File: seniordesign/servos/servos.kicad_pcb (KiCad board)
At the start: 2 copper layers, 77.5 x 38.1 mm, 24 parts, among them CON1 USB-MICRO-B, P1 SERVO_PWMS, U1 FT234XD, U2 MSP430G2153, U3 ADP151AUJZ-3.3-R7, U4 SN74LV1T04, U5 SN74LV1T04, U6 SN74LV1T04, U7 SN74LV1T04

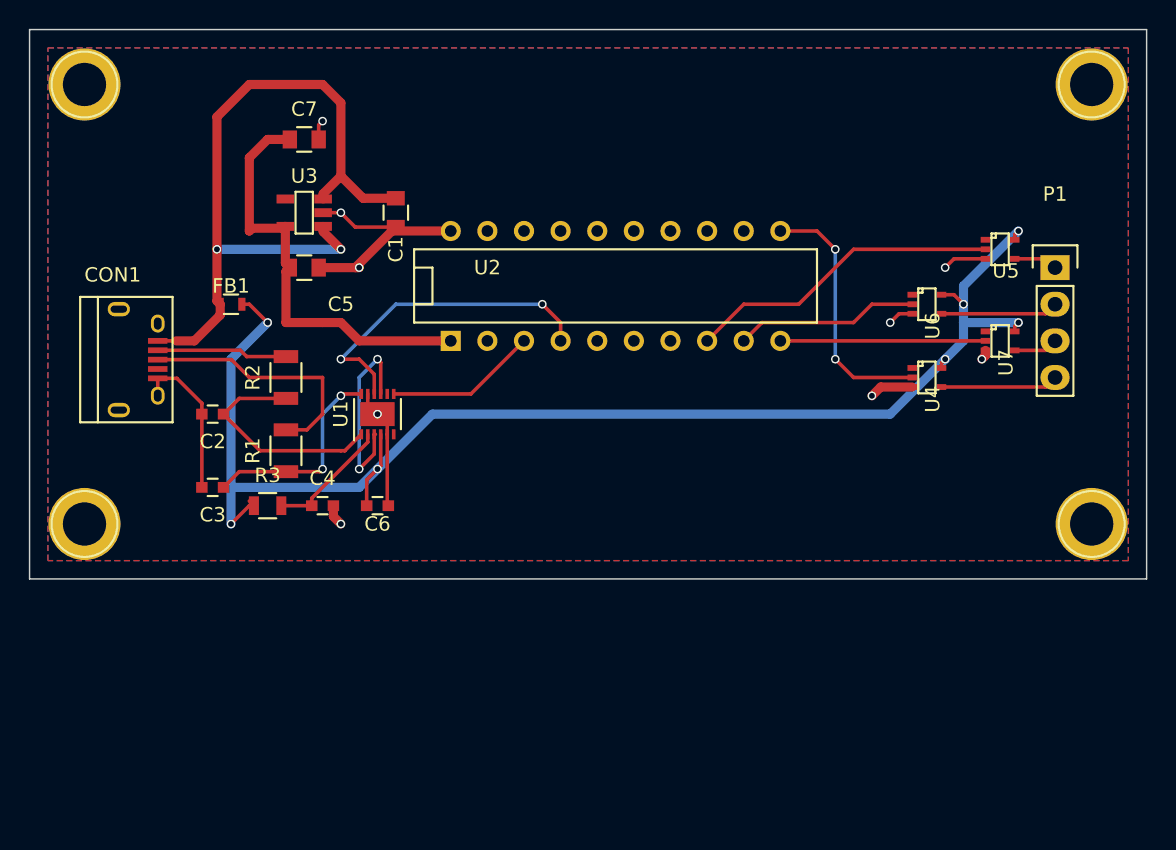
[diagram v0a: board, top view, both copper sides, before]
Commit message: Fix servo stuff, regenerate Gerber files for everything
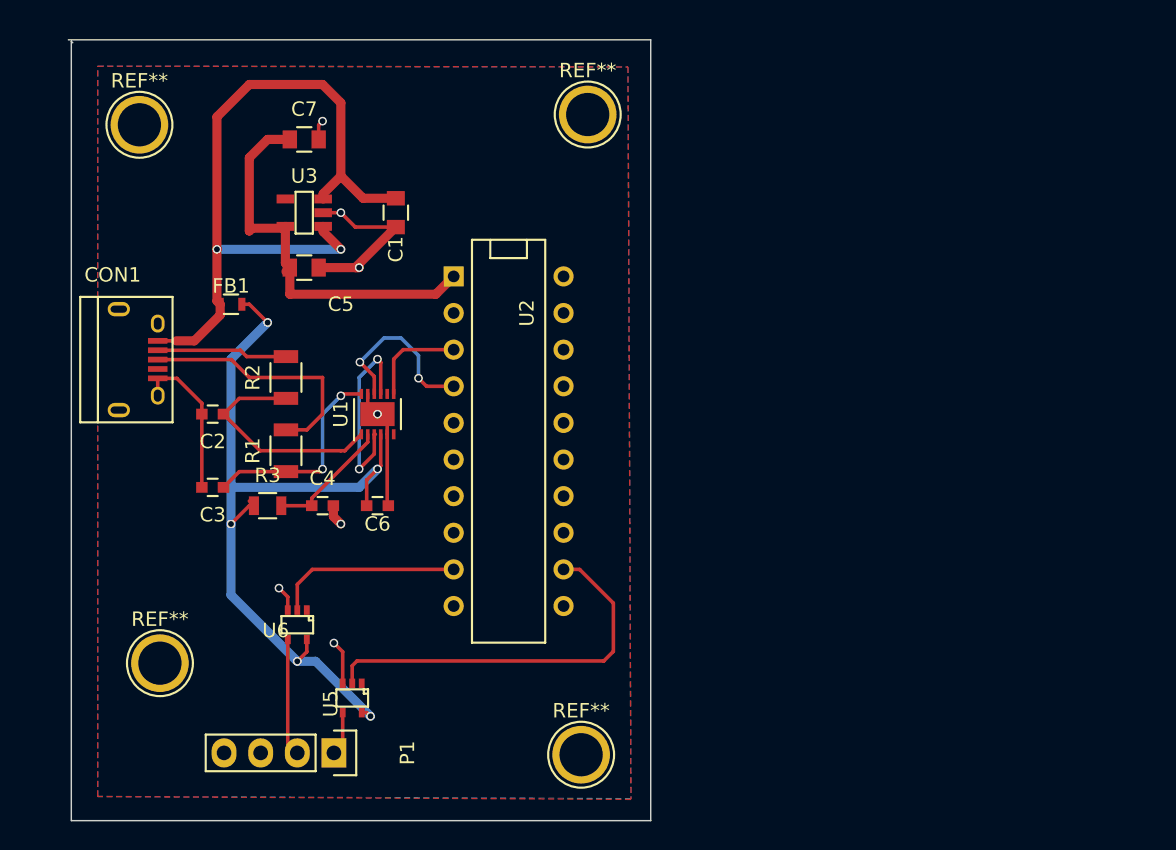
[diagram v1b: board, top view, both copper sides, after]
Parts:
- removed the REF** at (104.1, 61.0)
- removed the REF** at (104.1, 91.4)
- removed the REF** at (174.0, 91.4)
- removed the REF** at (174.0, 61.0)
- removed U4, U7: SN74LV1T04, Transistors_SMD:sc70-5
- added REF**: 1pin, Connect:1pin, F.Cu at (109.4, 101.1)
- added REF**: 1pin, Connect:1pin, F.Cu at (138.6, 107.4)
- added REF**: 1pin, Connect:1pin, F.Cu at (139.0, 63.0)
- added REF**: 1pin, Connect:1pin, F.Cu at (108.0, 63.8)
- moved P1 60.3 mm to (121.4, 107.3), turned to 270 degrees
- moved U5 54.7 mm to (122.7, 103.5), turned to 180 degrees
- moved U6 49.0 mm to (118.9, 98.4), turned to 180 degrees
- moved U2 13.1 mm to (133.6, 85.7), turned to 270 degrees
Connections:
- CON1 pad 4: Net-(CON1-Pad4) -> (no net)
- P1 pad 3: Net-(P1-Pad3) -> (no net)
- P1 pad 4: Net-(P1-Pad4) -> (no net)
- U1 pad 6: Net-(U1-Pad6) -> (no net)
- U1 pad 8: Net-(U1-Pad8) -> (no net)
- U2 pad 10: Net-(U2-Pad10) -> (no net)
- U2 pad 11: Net-(U2-Pad11) -> (no net)
- U2 pad 13: Net-(U2-Pad13) -> (no net)
- U2 pad 14: Net-(U2-Pad14) -> (no net)
- U2 pad 15: Net-(U2-Pad15) -> (no net)
- U2 pad 18: Net-(U2-Pad18) -> (no net)
- U2 pad 19: Net-(U2-Pad19) -> (no net)
- U2 pad 2: Net-(U2-Pad2) -> (no net)
- U2 pad 5: Net-(U2-Pad5) -> (no net)
- U2 pad 6: Net-(U2-Pad6) -> (no net)
- U2 pad 7: Net-(U2-Pad7) -> (no net)
- U2 pad 8: Net-(U2-Pad8) -> (no net)
- U3 pad 4: Net-(U3-Pad4) -> (no net)
- U5 pad 2: Net-(U2-Pad8) -> Net-(U2-Pad12)
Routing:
- net +5V: track 97.2 -> 56.5 mm, vias 7 -> 5
- net Net-(U2-Pad12): track 0.00 -> 27.5 mm
- net Net-(U2-Pad8): track 21.9 -> 0.00 mm
- net Net-(U2-Pad11): track 17.8 -> 0.00 mm, vias 2 -> 0
- net Net-(U2-Pad10): track 14.2 -> 0.00 mm
- net Net-(U1-Pad10): track 22.7 -> 12.1 mm
- net Net-(P1-Pad4): track 8.15 -> 0.00 mm
- net GND: track 48.2 -> 40.3 mm, vias 9 -> 7
- net Net-(U1-Pad7): track 10.6 -> 6.85 mm
- net Net-(P1-Pad3): track 3.07 -> 0.00 mm
- net Net-(C5-Pad1): track 30.0 -> 28.2 mm
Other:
- board size 77.5 x 38.1 mm -> 40.4 x 54.2 mm
